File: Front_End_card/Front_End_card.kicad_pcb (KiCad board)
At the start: 2 copper layers, 128 x 70 mm, 21 parts, among them J1 CONN_01X03, J2 CONN_01X03, J3 CONN_01X02, J4 CONN_01X02, J5 CONN_01X02, J6 CONN_01X04, U1 ACS758xCB-PFF, U2 ACS758xCB-PFF, U3 ACS758xCB-PFF

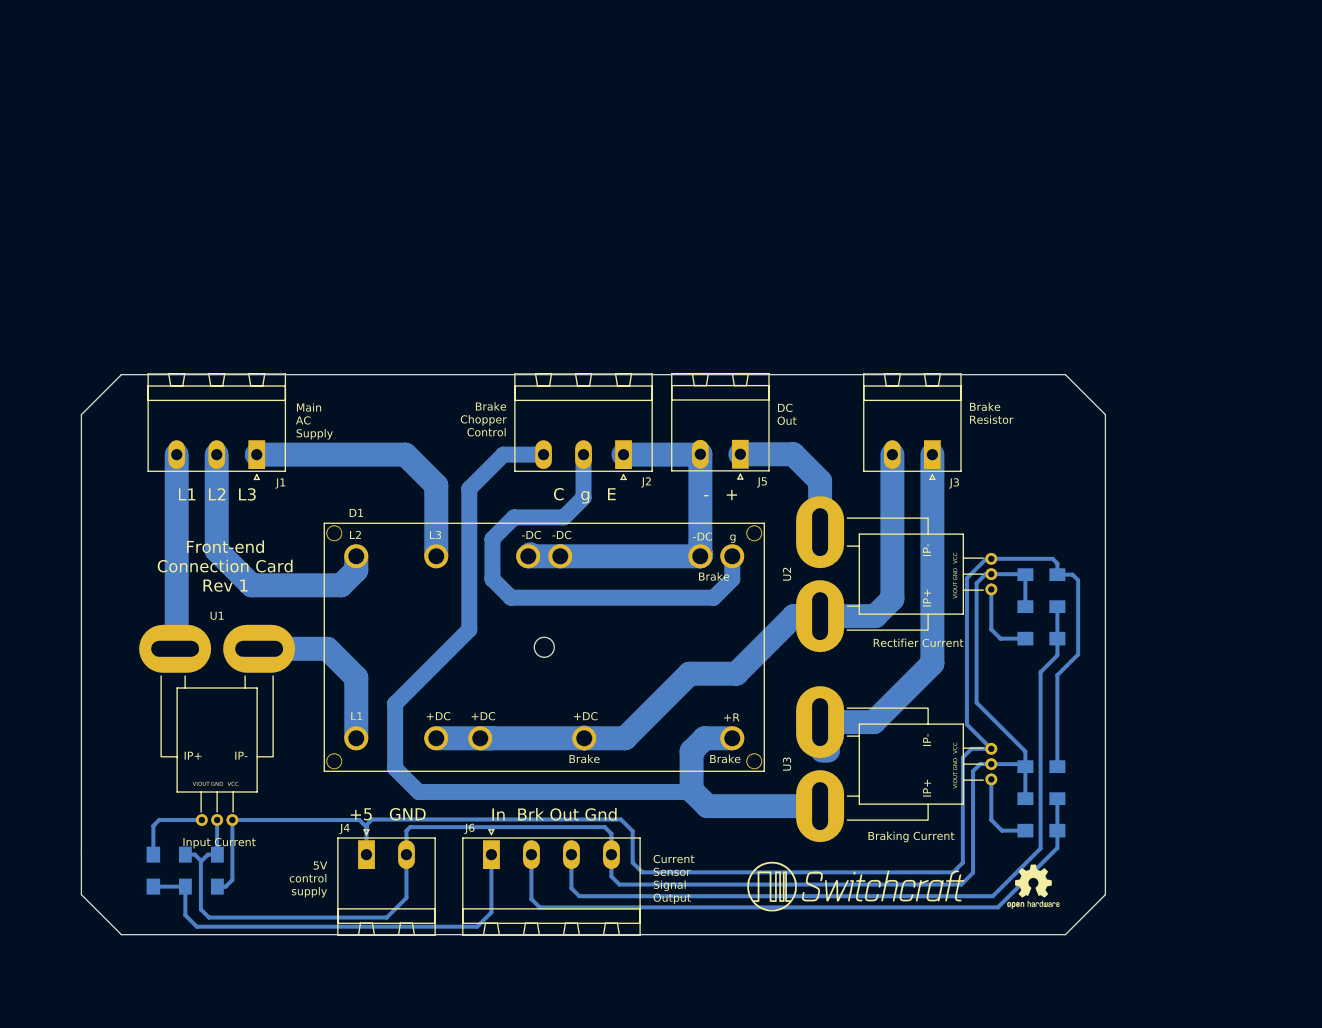
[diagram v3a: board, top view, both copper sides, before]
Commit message: Added final touch to silkscreen
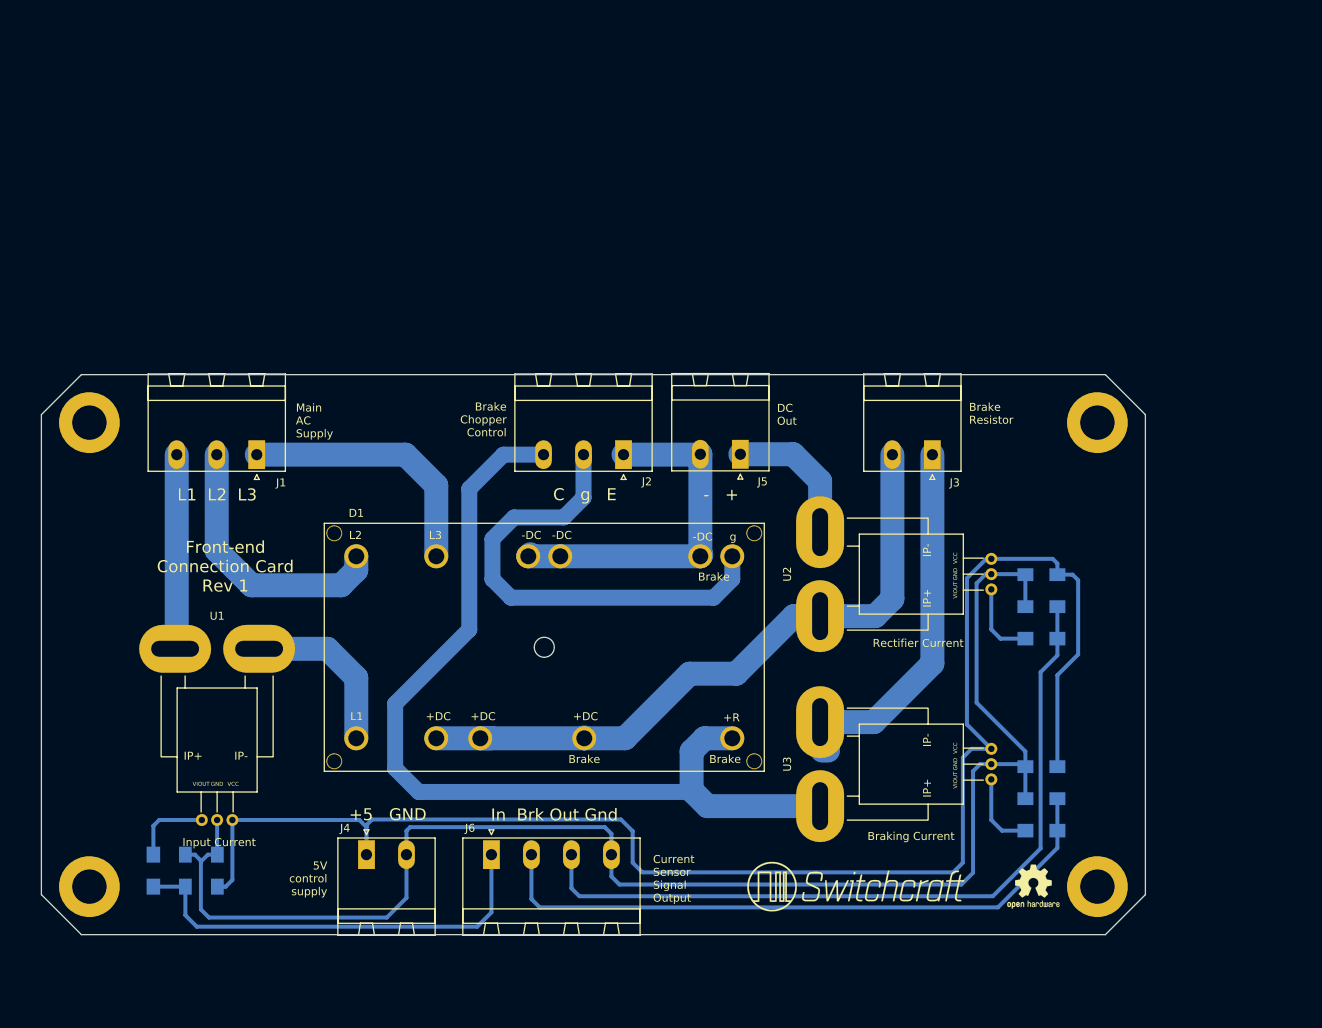
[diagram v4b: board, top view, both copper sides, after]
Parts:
- added REF**: MountingHole_4.3mm_M4_ISO7380_Pad, Mounting_Holes:MountingHole_4.3mm_M4_ISO7380_Pad, F.Cu at (93.0, 104.0)
- added REF**: MountingHole_4.3mm_M4_ISO7380_Pad, Mounting_Holes:MountingHole_4.3mm_M4_ISO7380_Pad, F.Cu at (93.0, 162.0)
- added REF**: MountingHole_4.3mm_M4_ISO7380_Pad, Mounting_Holes:MountingHole_4.3mm_M4_ISO7380_Pad, F.Cu at (219.0, 162.0)
- added REF**: MountingHole_4.3mm_M4_ISO7380_Pad, Mounting_Holes:MountingHole_4.3mm_M4_ISO7380_Pad, F.Cu at (219.0, 104.0)
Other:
- board size 128 x 70 mm -> 138 x 70 mm
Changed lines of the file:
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@@
     (links 42)
     (no_connects 0)
-    (area 91.949999 97.949999 220.050001 168.050001)
+    (area 86.949999 97.949999 225.050001 168.050001)
     (thickness 1.6)
-    (drawings 29)
+    (drawings 28)
     (tracks 158)
     (zones 0)
-    (modules 21)
+    (modules 25)
     (nets 19)
   )
@@
     (add_net "Net-(R2-Pad2)")
     (add_net "Net-(R3-Pad2)")
+  )
+  (module Mounting_Holes:MountingHole_4.3mm_M4_ISO7380_Pad (layer F.Cu)
+    (at 93 104)
+    (descr "Mounting Hole 4.3mm, M4, ISO7380")
+    (tags "mounting hole 4.3mm m4 iso7380")
+    (fp_text reference REF** (at 0 -4.8) (layer F.SilkS) hide
+      (effects (font (size 1 1) (thickness 0.15)))
+    )
+    (fp_text value MountingHole_4.3mm_M4_ISO7380_Pad (at 0 4.8) (layer F.Fab)
+      (effects (font (size 1 1) (thickness 0.15)))
+    )
+    (fp_circle (center 0 0) (end 3.8 0) (layer Cmts.User) (width 0.15))
+    (fp_circle (center 0 0) (end 4.05 0) (layer F.CrtYd) (width 0.05))
+    (pad 1 thru_hole circle (at 0 0) (size 7.6 7.6) (drill 4.3) (layers *.Cu *.Mask))
+  )
+  (module Mounting_Holes:MountingHole_4.3mm_M4_ISO7380_Pad (layer F.Cu)
+    (at 93 162)
+    (descr "Mounting Hole 4.3mm, M4, ISO7380")
+    (tags "mounting hole 4.3mm m4 iso7380")
+    (fp_text reference REF** (at 0 -4.8) (layer F.SilkS) hide
+      (effects (font (size 1 1) (thickness 0.15)))
+    )
+    (fp_text value MountingHole_4.3mm_M4_ISO7380_Pad (at 0 4.8) (layer F.Fab)
+      (effects (font (size 1 1) (thickness 0.15)))
+    )
+    (fp_circle (center 0 0) (end 3.8 0) (layer Cmts.User) (width 0.15))
+    (fp_circle (center 0 0) (end 4.05 0) (layer F.CrtYd) (width 0.05))
+    (pad 1 thru_hole circle (at 0 0) (size 7.6 7.6) (drill 4.3) (layers *.Cu *.Mask))
+  )
+  (module Mounting_Holes:MountingHole_4.3mm_M4_ISO7380_Pad (layer F.Cu)
+    (at 219 162)
+    (descr "Mounting Hole 4.3mm, M4, ISO7380")
+    (tags "mounting hole 4.3mm m4 iso7380")
+    (fp_text reference REF** (at 0 -4.8) (layer F.SilkS) hide
+      (effects (font (size 1 1) (thickness 0.15)))
+    )
+    (fp_text value MountingHole_4.3mm_M4_ISO7380_Pad (at 0 4.8) (layer F.Fab)
+      (effects (font (size 1 1) (thickness 0.15)))
+    )
+    (fp_circle (center 0 0) (end 3.8 0) (layer Cmts.User) (width 0.15))
+    (fp_circle (center 0 0) (end 4.05 0) (layer F.CrtYd) (width 0.05))
+    (pad 1 thru_hole circle (at 0 0) (size 7.6 7.6) (drill 4.3) (layers *.Cu *.Mask))
   )
   (module Capacitors_SMD:C_1206_HandSoldering (layer B.Cu)
@@
     )
   )
+  (module Mounting_Holes:MountingHole_4.3mm_M4_ISO7380_Pad (layer F.Cu)
+    (at 219 104)
+    (descr "Mounting Hole 4.3mm, M4, ISO7380")
+    (tags "mounting hole 4.3mm m4 iso7380")
+    (fp_text reference REF** (at 0 -4.8) (layer F.SilkS) hide
+      (effects (font (size 1 1) (thickness 0.15)))
+    )
+    (fp_text value MountingHole_4.3mm_M4_ISO7380_Pad (at 0 4.8) (layer F.Fab)
+      (effects (font (size 1 1) (thickness 0.15)))
+    )
+    (fp_circle (center 0 0) (end 3.8 0) (layer Cmts.User) (width 0.15))
+    (fp_circle (center 0 0) (end 4.05 0) (layer F.CrtYd) (width 0.05))
+    (pad 1 thru_hole circle (at 0 0) (size 7.6 7.6) (drill 4.3) (layers *.Cu *.Mask))
+  )
+  (dimension 138 (width 0.3) (layer Dwgs.User)
+    (gr_text "138.000 mm" (at 156 92.65) (layer Dwgs.User)
+      (effects (font (size 1.5 1.5) (thickness 0.3)))
+    )
+    (feature1 (pts (xy 87 103) (xy 87 91.3)))
+    (feature2 (pts (xy 225 103) (xy 225 91.3)))
+    (crossbar (pts (xy 225 94) (xy 87 94)))
+    (arrow1a (pts (xy 87 94) (xy 88.126504 93.413579)))
+    (arrow1b (pts (xy 87 94) (xy 88.126504 94.586421)))
+    (arrow2a (pts (xy 225 94) (xy 223.873496 93.413579)))
+    (arrow2b (pts (xy 225 94) (xy 223.873496 94.586421)))
+  )
+  (dimension 70 (width 0.3) (layer Dwgs.User)
+    (gr_text "70.000 mm" (at 228.35 133 270) (layer Dwgs.User)
+      (effects (font (size 1.5 1.5) (thickness 0.3)))
+    )
+    (feature1 (pts (xy 220 168) (xy 229.7 168)))
+    (feature2 (pts (xy 220 98) (xy 229.7 98)))
+    (crossbar (pts (xy 227 98) (xy 227 168)))
+    (arrow1a (pts (xy 227 168) (xy 226.413579 166.873496)))
+    (arrow1b (pts (xy 227 168) (xy 227.586421 166.873496)))
+    (arrow2a (pts (xy 227 98) (xy 226.413579 99.126504)))
+    (arrow2b (pts (xy 227 98) (xy 227.586421 99.126504)))
+  )
   (gr_text "I have a million ideas. They all point to certain death." (at 141 165) (layer B.SilkS)
     (effects (font (size 0.75 0.75) (thickness 0.1875)) (justify mirror))
   )
-  (dimension 70 (width 0.3) (layer Dwgs.User)
-    (gr_text "70.000 mm" (at 225.35 133 270) (layer Dwgs.User)
-      (effects (font (size 1.5 1.5) (thickness 0.3)))
-    )
-    (feature1 (pts (xy 215 168) (xy 226.7 168)))
-    (feature2 (pts (xy 215 98) (xy 226.7 98)))
-    (crossbar (pts (xy 224 98) (xy 224 168)))
-    (arrow1a (pts (xy 224 168) (xy 223.413579 166.873496)))
-    (arrow1b (pts (xy 224 168) (xy 224.586421 166.873496)))
-    (arrow2a (pts (xy 224 98) (xy 223.413579 99.126504)))
-    (arrow2b (pts (xy 224 98) (xy 224.586421 99.126504)))
-  )
-  (dimension 128 (width 0.3) (layer Dwgs.User)
-    (gr_text "128.000 mm" (at 156 93.65) (layer Dwgs.User)
-      (effects (font (size 1.5 1.5) (thickness 0.3)))
-    )
-    (feature1 (pts (xy 220 103) (xy 220 92.3)))
-    (feature2 (pts (xy 92 103) (xy 92 92.3)))
-    (crossbar (pts (xy 92 95) (xy 220 95)))
-    (arrow1a (pts (xy 220 95) (xy 218.873496 95.586421)))
-    (arrow1b (pts (xy 220 95) (xy 218.873496 94.413579)))
-    (arrow2a (pts (xy 92 95) (xy 93.126504 95.586421)))
-    (arrow2b (pts (xy 92 95) (xy 93.126504 94.413579)))
-  )
-  (gr_line (start 220 163) (end 215 168) (angle 90) (layer Edge.Cuts) (width 0.1))
-  (gr_line (start 215 98) (end 220 103) (angle 90) (layer Edge.Cuts) (width 0.1))
-  (gr_line (start 92 163) (end 92 158) (angle 90) (layer Edge.Cuts) (width 0.1))
-  (gr_line (start 97 168) (end 92 163) (angle 90) (layer Edge.Cuts) (width 0.1))
-  (gr_line (start 92 103) (end 92 158) (angle 90) (layer Edge.Cuts) (width 0.1))
-  (gr_line (start 97 98) (end 92 103) (angle 90) (layer Edge.Cuts) (width 0.1))
-  (gr_line (start 215 168) (end 97 168) (angle 90) (layer Edge.Cuts) (width 0.1))
-  (gr_line (start 220 103) (end 220 163) (angle 90) (layer Edge.Cuts) (width 0.1))
-  (gr_line (start 97 98) (end 215 98) (angle 90) (layer Edge.Cuts) (width 0.1))
+  (gr_line (start 225 163) (end 220 168) (angle 90) (layer Edge.Cuts) (width 0.1))
+  (gr_line (start 220 98) (end 225 103) (angle 90) (layer Edge.Cuts) (width 0.1))
+  (gr_line (start 92 168) (end 87 163) (angle 90) (layer Edge.Cuts) (width 0.1))
+  (gr_line (start 87 103) (end 87 163) (angle 90) (layer Edge.Cuts) (width 0.1))
+  (gr_line (start 92 98) (end 87 103) (angle 90) (layer Edge.Cuts) (width 0.1))
+  (gr_line (start 220 168) (end 92 168) (angle 90) (layer Edge.Cuts) (width 0.1))
+  (gr_line (start 225 103) (end 225 163) (angle 90) (layer Edge.Cuts) (width 0.1))
+  (gr_line (start 92 98) (end 220 98) (angle 90) (layer Edge.Cuts) (width 0.1))
   (gr_text "Input Current" (at 109.22 156.464) (layer F.SilkS)
     (effects (font (size 1 1) (thickness 0.25)))
@@
   (segment (start 202.692 123.444) (end 202.692 141.727) (width 0.5) (layer B.Cu) (net 1))
   (segment (start 106.934 158.877) (end 106.934 158.75) (width 0.5) (layer B.Cu) (net 2))
-  (segment (start 106.184 158) (end 105 158) (width 0.5) (layer B.Cu) (net 2) (status 800000))
+  (segment (start 106.184 158) (end 105 158) (width 0.5) (layer B.Cu) (net 2))
   (segment (start 106.934 158.75) (end 106.184 158) (width 0.5) (layer B.Cu) (net 2))
   (segment (start 132.635 158) (end 132.635 163.402) (width 0.5) (layer B.Cu) (net 2))
